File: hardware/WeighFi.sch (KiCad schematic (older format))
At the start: 0 parts

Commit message: Battery charging and power supply components added to schematic
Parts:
- added BT1: BATTERY, symbol BATTERY
- added C1, C2, C3, C4, C5: 1uF, symbol C
- added H1, H2, H3, H4: HOLE, symbol HOLE
- added ISP1: AVR-ISP-6, AVR-ISP-6, symbol AVR-ISP-6
- added J1: USB, symbol USB
- added P1, P2, P3: CONN_1, symbol CONN_1
- added U1: MAX1555, symbol MAX1555
- added U2: MCP1700, symbol MCP1700
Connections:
- net labels added: +3V, +BATT, +VUSB, CHG, D+, D-, GND, MISO, MOSI, RST, SCK
- wire segments 0 -> 38
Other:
- note added: "In System Programming"
- note added: "Mounting holes"
- note added: "USB, LiPo charging, and power supply"

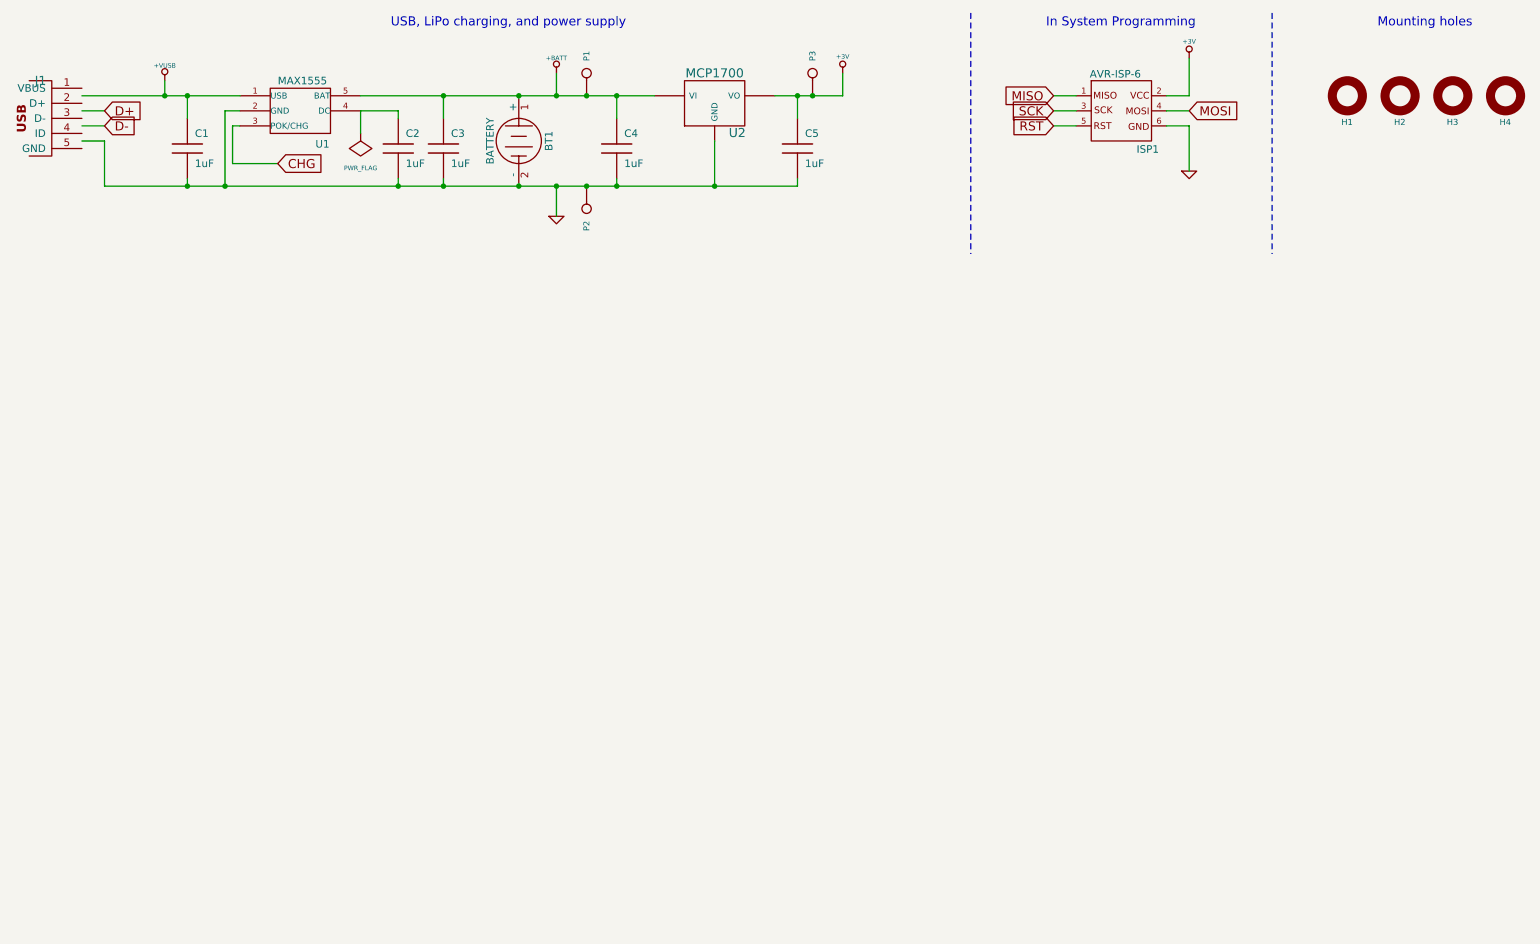
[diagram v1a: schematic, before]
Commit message: Added LCD driver IC and panel connector to schematic
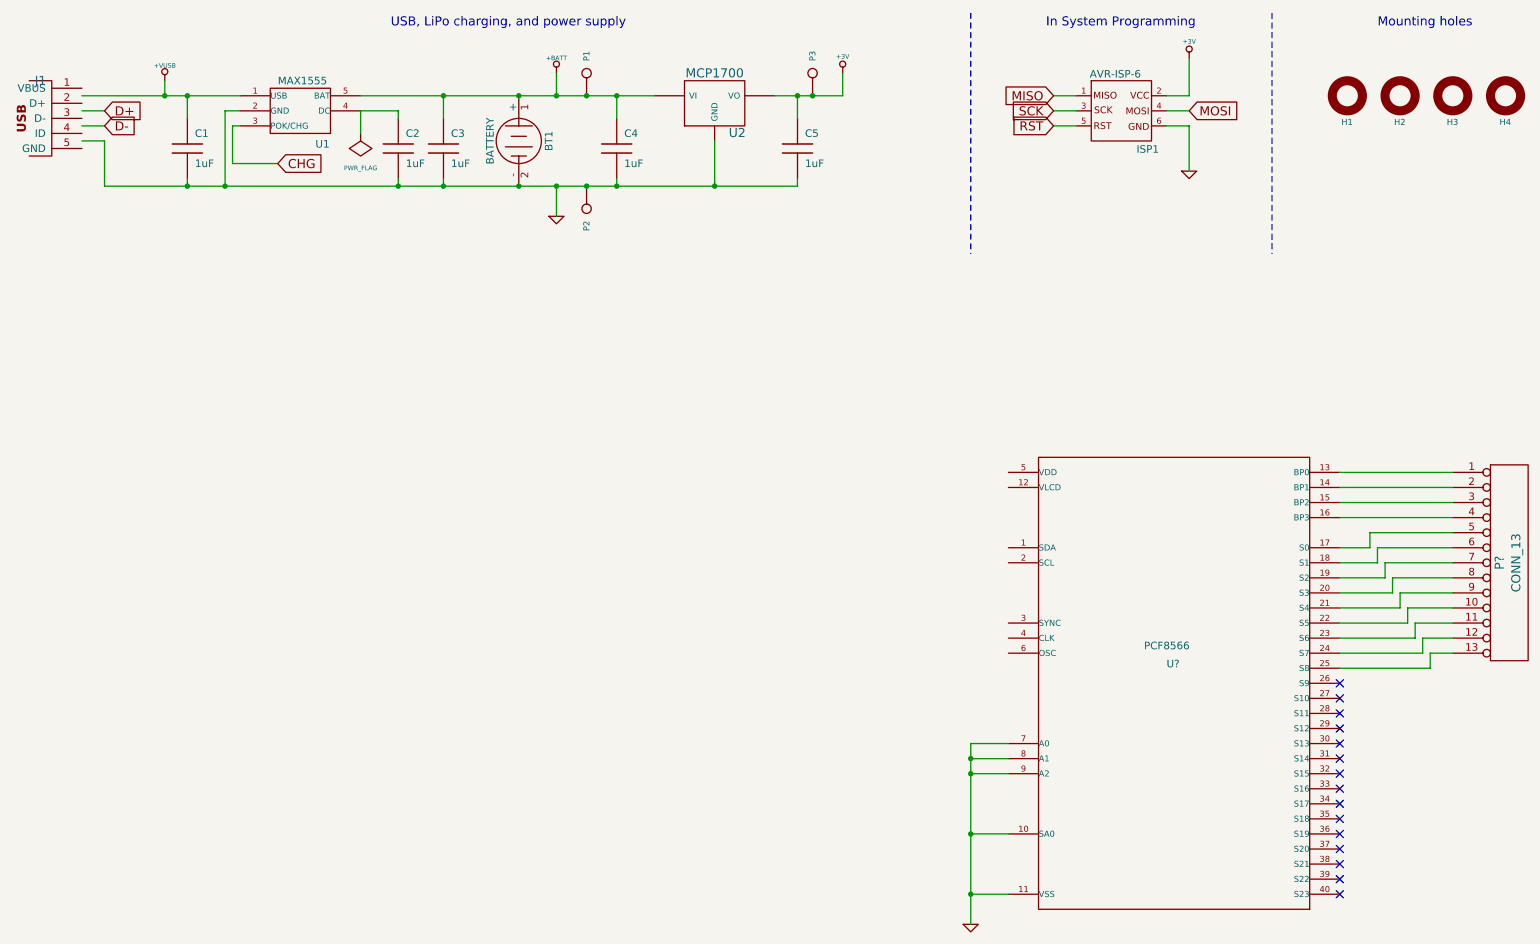
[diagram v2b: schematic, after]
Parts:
- added P?: CONN_13, symbol CONN_13
- added U?: PCF8566, symbol PCF8566
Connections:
- wire segments 38 -> 75
- no-connect marks 0 -> 15
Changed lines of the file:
@@
-EESchema Schematic File Version 2  date Sat 28 Apr 2012 18:56:34 BST
+EESchema Schematic File Version 2  date Thu 10 May 2012 13:00:41 BST
 LIBS:dresco
 LIBS:power
@@
 Sheet 1 1
 Title "WeighFi"
-Date "28 apr 2012"
+Date "10 may 2012"
 Rev "1.0"
 Comp ""
@@
 Comment4 ""
 $EndDescr
+Connection ~ 7100 6450
+Wire Wire Line
+	7350 6450 7100 6450
+Connection ~ 7100 5650
+Wire Wire Line
+	7350 5650 7100 5650
+Wire Wire Line
+	7100 6650 7100 5450
+Wire Wire Line
+	7100 5450 7350 5450
+Wire Wire Line
+	9550 4850 10100 4850
+Wire Wire Line
+	10100 4850 10100 4750
+Wire Wire Line
+	10100 4750 10300 4750
+Wire Wire Line
+	9550 4650 10000 4650
+Wire Wire Line
+	10000 4650 10000 4550
+Wire Wire Line
+	10000 4550 10300 4550
+Wire Wire Line
+	9550 4450 9900 4450
+Wire Wire Line
+	9900 4450 9900 4350
+Wire Wire Line
+	9900 4350 10300 4350
+Wire Wire Line
+	9550 4250 9800 4250
+Wire Wire Line
+	9800 4250 9800 4150
+Wire Wire Line
+	9800 4150 10300 4150
+Wire Wire Line
+	10300 3950 9550 3950
+Wire Wire Line
+	9550 3750 10300 3750
+Connection ~ 4100 1150
+Wire Wire Line
+	5000 1150 3050 1150
+Wire Notes Line
+	7100 600  7100 2200
+Wire Wire Line
+	1350 1450 1350 1750
+Wire Wire Line
+	1350 1450 1200 1450
+Wire Wire Line
+	1200 1350 1350 1350
+Wire Wire Line
+	1750 1150 1750 1050
+Wire Wire Line
+	2150 1750 2150 1250
+Wire Wire Line
+	2150 1250 2250 1250
+Connection ~ 1900 1750
+Connection ~ 3300 1750
+Wire Wire Line
+	3300 1750 3300 1700
+Connection ~ 3600 1150
+Wire Wire Line
+	3600 1150 3600 1300
+Wire Wire Line
+	1900 1300 1900 1150
+Connection ~ 4550 1750
+Connection ~ 4550 1150
+Connection ~ 6050 1150
+Wire Wire Line
+	8550 1650 8550 1350
+Wire Wire Line
+	8550 1350 8400 1350
+Wire Wire Line
+	7800 1350 7650 1350
+Wire Wire Line
+	7800 1150 7650 1150
+Connection ~ 4750 1150
+Connection ~ 5950 1150
+Wire Wire Line
+	5950 1150 5950 1300
+Connection ~ 4750 1750
+Wire Wire Line
+	4750 1750 4750 1700
+Connection ~ 4350 1750
+Wire Wire Line
+	4350 1750 4350 1950
+Wire Wire Line
+	6250 1000 6250 1150
+Wire Wire Line
+	5400 1750 5400 1450
+Connection ~ 5400 1750
+Wire Wire Line
+	4350 1150 4350 1000
+Connection ~ 4350 1150
+Wire Wire Line
+	5950 1700 5950 1750
+Wire Wire Line
+	6250 1150 5800 1150
+Wire Wire Line
+	7800 1250 7650 1250
+Wire Wire Line
+	8400 1250 8550 1250
+Wire Wire Line
+	8400 1150 8550 1150
+Wire Wire Line
+	8550 1150 8550 900
+Wire Wire Line
+	4750 1300 4750 1150
+Connection ~ 2150 1750
+Wire Wire Line
+	3300 1250 3050 1250
+Wire Wire Line
+	3300 1250 3300 1300
+Wire Wire Line
+	3600 1750 3600 1700
+Wire Wire Line
+	1900 1700 1900 1750
+Connection ~ 1900 1150
+Wire Wire Line
+	2250 1350 2200 1350
+Wire Wire Line
+	2200 1350 2200 1600
+Wire Wire Line
+	2200 1600 2500 1600
+Wire Wire Line
+	1200 1250 1350 1250
+Wire Wire Line
+	2250 1150 1200 1150
+Connection ~ 1750 1150
+Wire Notes Line
+	9100 600  9100 2200
+Wire Wire Line
+	5950 1750 1350 1750
+Connection ~ 3600 1750
+Connection ~ 4100 1750
+Wire Wire Line
+	3050 1250 3050 1400
+Wire Wire Line
+	10300 3650 9550 3650
+Wire Wire Line
+	10300 3850 9550 3850
+Wire Wire Line
+	10300 4050 9750 4050
+Wire Wire Line
+	9750 4050 9750 4150
+Wire Wire Line
+	9750 4150 9550 4150
+Wire Wire Line
+	10300 4250 9850 4250
+Wire Wire Line
+	9850 4250 9850 4350
+Wire Wire Line
+	9850 4350 9550 4350
+Wire Wire Line
+	10300 4450 9950 4450
+Wire Wire Line
+	9950 4450 9950 4550
+Wire Wire Line
+	9950 4550 9550 4550
+Wire Wire Line
+	10300 4650 10050 4650
+Wire Wire Line
+	10050 4650 10050 4750
+Wire Wire Line
+	10050 4750 9550 4750
+Wire Wire Line
+	10300 4850 10150 4850
+Wire Wire Line
+	10150 4850 10150 4950
+Wire Wire Line
+	10150 4950 9550 4950
+Wire Wire Line
+	7350 5550 7100 5550
+Connection ~ 7100 5550
+Wire Wire Line
+	7350 6050 7100 6050
+Connection ~ 7100 6050
+$Comp
+L GND #PWR?
+U 1 1 4FABACF9
+P 7100 6650
+F 0 "#PWR?" H 7100 6650 30  0001 C CNN
+F 1 "GND" H 7100 6580 30  0001 C CNN
+	1    7100 6650
+	1    0    0    -1
+$EndComp
+NoConn ~ 9550 6450
+NoConn ~ 9550 6350
+NoConn ~ 9550 6250
+NoConn ~ 9550 6150
+NoConn ~ 9550 6050
+NoConn ~ 9550 5950
+NoConn ~ 9550 5850
+NoConn ~ 9550 5750
+NoConn ~ 9550 5650
+NoConn ~ 9550 5550
+NoConn ~ 9550 5450
+NoConn ~ 9550 5350
+NoConn ~ 9550 5250
+NoConn ~ 9550 5150
+NoConn ~ 9550 5050
+$Comp
+L PCF8566 U?
+U 1 1 4F9EC09D
+P 8450 5050
+F 0 "U?" H 8400 5150 50  0000 L BNN
+F 1 "PCF8566" H 8250 5270 50  0000 L BNN
+	1    8450 5050
+	1    0    0    -1
+$EndComp
+$Comp
+L CONN_13 P?
+U 1 1 4F9EC08F
+P 10650 4250
+F 0 "P?" V 10610 4250 60  0000 C CNN
+F 1 "CONN_13" V 10720 4250 60  0000 C CNN
+	1    10650 4250
+	1    0    0    -1
+$EndComp
 $Comp
 L MCP1700 U2
@@
 	1    0    0    -1
 $EndComp
-Connection ~ 4100 1150
-Wire Wire Line
-	3050 1150 5000 1150
-Wire Notes Line
-	7100 600  7100 2200
-Wire Wire Line
-	1350 1450 1350 1750
-Wire Wire Line
-	1350 1450 1200 1450
-Wire Wire Line
-	1200 1350 1350 1350
-Wire Wire Line
-	1750 1050 1750 1150
-Wire Wire Line
-	2150 1750 2150 1250
-Wire Wire Line
-	2150 1250 2250 1250
-Connection ~ 1900 1750
-Connection ~ 3300 1750
-Wire Wire Line
-	3300 1750 3300 1700
-Connection ~ 3600 1150
-Wire Wire Line
-	3600 1150 3600 1300
-Wire Wire Line
-	1900 1150 1900 1300
-Connection ~ 4550 1750
-Connection ~ 4550 1150
-Connection ~ 6050 1150
-Wire Wire Line
-	8550 1650 8550 1350
-Wire Wire Line
-	8550 1350 8400 1350
-Wire Wire Line
-	7800 1350 7650 1350
-Wire Wire Line
-	7800 1150 7650 1150
-Connection ~ 4750 1150
-Connection ~ 5950 1150
-Wire Wire Line
-	5950 1150 5950 1300
-Connection ~ 4750 1750
-Wire Wire Line
-	4750 1750 4750 1700
-Connection ~ 4350 1750
-Wire Wire Line
-	4350 1750 4350 1950
-Wire Wire Line
-	6250 1000 6250 1150
-Wire Wire Line
-	5400 1450 5400 1750
-Connection ~ 5400 1750
-Wire Wire Line
-	4350 1150 4350 1000
-Connection ~ 4350 1150
-Wire Wire Line
-	5950 1700 5950 1750
-Wire Wire Line
-	6250 1150 5800 1150
-Wire Wire Line
-	7800 1250 7650 1250
-Wire Wire Line
-	8400 1250 8550 1250
-Wire Wire Line
-	8400 1150 8550 1150
-Wire Wire Line
-	8550 1150 8550 900
-Wire Wire Line
-	4750 1300 4750 1150
-Connection ~ 2150 1750
-Wire Wire Line
-	3300 1250 3050 1250
-Wire Wire Line
-	3300 1250 3300 1300
-Wire Wire Line
-	3600 1750 3600 1700
-Wire Wire Line
-	1900 1750 1900 1700
-Connection ~ 1900 1150
-Wire Wire Line
-	2250 1350 2200 1350
-Wire Wire Line
-	2200 1350 2200 1600
-Wire Wire Line
-	2200 1600 2500 1600
-Wire Wire Line
-	1200 1250 1350 1250
-Wire Wire Line
-	1200 1150 2250 1150
-Connection ~ 1750 1150
-Wire Notes Line
-	9100 600  9100 2200
-Wire Wire Line
-	5950 1750 1350 1750
-Connection ~ 3600 1750
-Connection ~ 4100 1750
-Wire Wire Line
-	3050 1250 3050 1400
 $Comp
 L PWR_FLAG #FLG01
